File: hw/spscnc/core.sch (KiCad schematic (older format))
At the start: 55 parts, among them J11 Conn_01x04, J7 USB_B_Micro, Q11 BSP41, Q12 BSP42, U13 74HC595, U14 74HC595, U3 NCP1117ST33T3G, U4 ESP32-WROOM-32D, U8 FT232RL

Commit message: Finished preliminary routing, pending checklist and review
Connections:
- net labels added: LIM_A, LIM_B
- wire segments 118 -> 120
- no-connect marks 21 -> 19
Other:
- note removed: "CHECKS:\n[OK] change fluidnc config and attempt to boot.\n[OK] check bootmode is ok with GPIO signals\ncheck pulses during boot on output pins.\n"
- note removed: "DRV8825 design used io15 for the door\n"
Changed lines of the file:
@@
 	1    0    0    -1
 $EndComp
-Text Notes 5275 8450 0    50   ~ 0
-DRV8825 design used io15 for the door\n
 Text GLabel 7425 1975 2    39   Output ~ 0
 ~STEPPER_CS
@@
 	-1   0    0    -1
 $EndComp
-Text Notes 12650 3350 0    50   ~ 0
+Text Notes 9075 4125 0    50   ~ 0
 BOOT MODE:\nMTDI 0 => 3v3 SPI\nGPIO0 1 => Boot APP\nGPIO2 0 => Download\nMTDO 0 => Silent UART / SDIO Sample Fall\nGPIO5 SDIO Launch Fall
-Text Notes 12525 3900 0    50   ~ 0
-CHECKS:\n[OK] change fluidnc config and attempt to boot.\n[OK] check bootmode is ok with GPIO signals\ncheck pulses during boot on output pins.\n
 Text GLabel 7775 1475 2    50   Output ~ 0
 SPINDLE_EN
@@
 Wire Wire Line
 	7575 1475 7775 1475
-Text GLabel 9750 5000 2    50   Output ~ 0
+Text GLabel 9750 5100 2    50   Output ~ 0
 DIR_A
 $Comp
@@
 Wire Wire Line
 	9550 5100 9750 5100
-Text GLabel 9750 5100 2    50   Output ~ 0
+Text GLabel 9750 5300 2    50   Output ~ 0
 STEP_A
 Wire Wire Line
@@
 Wire Wire Line
 	5425 5475 5425 5950
-Text GLabel 9750 5300 2    50   Output ~ 0
+Text GLabel 9750 5000 2    50   Output ~ 0
 DIR_B
 $Comp
@@
 	7550 5775 6400 5775
 NoConn ~ 9350 5700
-NoConn ~ 7325 1775
-NoConn ~ 7325 1875
 NoConn ~ 7375 2775
 $Comp
@@
 	1    0    0    -1
 $EndComp
+Text GLabel 7400 1775 2    50   Input ~ 0
+LIM_A
+Text GLabel 7400 1875 2    50   Input ~ 0
+LIM_B
+Wire Wire Line
+	7400 1775 7325 1775
+Wire Wire Line
+	7325 1875 7400 1875
 $EndSCHEMATC

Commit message: As ordered 1.0.1
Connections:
- wire segments 120 -> 123
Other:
- note added: "CRITICAL BOOT MODE:\nMTDI 0 => 3v3 SPI\nGPIO0 1 => Boot APP\nGPIO2 0 => Download\nMTDO 0 => Silent UART / SDIO Sample Fall\nGPIO5 SDIO Launch Falling edge.\n"
- note removed: "BOOT MODE:\nMTDI 0 => 3v3 SPI\nGPIO0 1 => Boot APP\nGPIO2 0 => Download\nMTDO 0 => Silent UART / SDIO Sample Fall\nGPIO5 SDIO Launch Fall"
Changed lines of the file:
@@
 Sheet 6 17
 Title "Trinamic FluidNC CNC Controller"
-Date "2022-01-27"
-Rev "1.0.0"
+Date "2022-02-12"
+Rev "1.0.1"
 Comp ""
 Comment1 ""
@@
 $EndComp
 Text Notes 9075 4125 0    50   ~ 0
-BOOT MODE:\nMTDI 0 => 3v3 SPI\nGPIO0 1 => Boot APP\nGPIO2 0 => Download\nMTDO 0 => Silent UART / SDIO Sample Fall\nGPIO5 SDIO Launch Fall
+CRITICAL BOOT MODE:\nMTDI 0 => 3v3 SPI\nGPIO0 1 => Boot APP\nGPIO2 0 => Download\nMTDO 0 => Silent UART / SDIO Sample Fall\nGPIO5 SDIO Launch Falling edge.\n
 Text GLabel 7775 1475 2    50   Output ~ 0
 SPINDLE_EN
 Text GLabel 8650 2875 2    50   Output ~ 0
 ENABLE_STEPPERS
-Text GLabel 7800 2075 2    50   Output ~ 0
+Text GLabel 8750 2075 2    50   Output ~ 0
 SPINDLE_PWM
 Text GLabel 9750 4800 2    50   Output ~ 0
@@
 Text Label 5600 5375 2    50   ~ 0
 I2S_WORDSTROBE
-$Comp
-L power:GND-power #PWR?
-U 1 1 62063E5C
-P 5600 5175
-AR Path="/5AD46BE5/62063E5C" Ref="#PWR?"  Part="1"
-AR Path="/5AD46BE5/619A452E/62063E5C" Ref="#PWR?"  Part="1"
-AR Path="/62063E5C" Ref="#PWR?"  Part="1"
-AR Path="/61B9A8A6/62063E5C" Ref="#PWR?"  Part="1"
-AR Path="/61C743E7/61B9A8A6/62063E5C" Ref="#PWR?"  Part="1"
-AR Path="/61C81F9D/62063E5C" Ref="#PWR024"  Part="1"
-F 0 "#PWR024" H 5600 4925 50  0001 C CNN
-F 1 "GND" H 5600 5025 50  0000 C CNN
-F 2 "" H 5600 5175 50  0001 C CNN
-F 3 "" H 5600 5175 50  0001 C CNN
-	1    5600 5175
-	0    1    -1   0
-$EndComp
 Text Label 5600 5475 2    50   ~ 0
 ~I2S_ENABLE
@@
 	9750 4800 9550 4800
 Wire Wire Line
-	7600 2075 7800 2075
+	7600 2075 8750 2075
 Wire Wire Line
 	7575 1475 7775 1475
@@
 Text Label 8550 5300 2    50   ~ 0
 I2S_WORDSTROBE
-$Comp
-L power:GND-power #PWR?
-U 1 1 620F09C1
-P 8550 5100
-AR Path="/5AD46BE5/620F09C1" Ref="#PWR?"  Part="1"
-AR Path="/5AD46BE5/619A452E/620F09C1" Ref="#PWR?"  Part="1"
-AR Path="/620F09C1" Ref="#PWR?"  Part="1"
-AR Path="/61B9A8A6/620F09C1" Ref="#PWR?"  Part="1"
-AR Path="/61C743E7/61B9A8A6/620F09C1" Ref="#PWR?"  Part="1"
-AR Path="/61C81F9D/620F09C1" Ref="#PWR083"  Part="1"
-F 0 "#PWR083" H 8550 4850 50  0001 C CNN
-F 1 "GND" H 8550 4950 50  0000 C CNN
-F 2 "" H 8550 5100 50  0001 C CNN
-F 3 "" H 8550 5100 50  0001 C CNN
-	1    8550 5100
-	0    1    -1   0
-$EndComp
 Text Label 8550 5400 2    50   ~ 0
 ~I2S_ENABLE
@@
 Wire Wire Line
 	7325 1875 7400 1875
+$Comp
+L power:+3.3VA-power #PWR?
+U 1 1 620826BE
+P 7975 5050
+AR Path="/61367F02/620826BE" Ref="#PWR?"  Part="1"
+AR Path="/5AD46BE5/619A452E/61B9A8A6/620826BE" Ref="#PWR?"  Part="1"
+AR Path="/61B9A8A6/620826BE" Ref="#PWR?"  Part="1"
+AR Path="/61C743E7/61B9A8A6/620826BE" Ref="#PWR?"  Part="1"
+AR Path="/61C81F9D/620826BE" Ref="#PWR?"  Part="1"
+AR Path="/620826BE" Ref="#PWR?"  Part="1"
+F 0 "#PWR?" H 7975 4900 50  0001 C CNN
+F 1 "+3.3VA" H 7975 5225 50  0000 C CNN
+F 2 "" H 7975 5050 50  0001 C CNN
+F 3 "" H 7975 5050 50  0001 C CNN
+	1    7975 5050
+	1    0    0    -1
+$EndComp
+Wire Wire Line
+	8550 5100 7975 5100
+Wire Wire Line
+	7975 5100 7975 5050
+$Comp
+L power:+3.3VA-power #PWR?
+U 1 1 6208D205
+P 5200 5175
+AR Path="/61367F02/6208D205" Ref="#PWR?"  Part="1"
+AR Path="/5AD46BE5/619A452E/61B9A8A6/6208D205" Ref="#PWR?"  Part="1"
+AR Path="/61B9A8A6/6208D205" Ref="#PWR?"  Part="1"
+AR Path="/61C743E7/61B9A8A6/6208D205" Ref="#PWR?"  Part="1"
+AR Path="/61C81F9D/6208D205" Ref="#PWR?"  Part="1"
+AR Path="/6208D205" Ref="#PWR?"  Part="1"
+F 0 "#PWR?" H 5200 5025 50  0001 C CNN
+F 1 "+3.3VA" V 5225 5425 50  0000 C CNN
+F 2 "" H 5200 5175 50  0001 C CNN
+F 3 "" H 5200 5175 50  0001 C CNN
+	1    5200 5175
+	0    -1   -1   0
+$EndComp
+Wire Wire Line
+	5200 5175 5600 5175
 $EndSCHEMATC

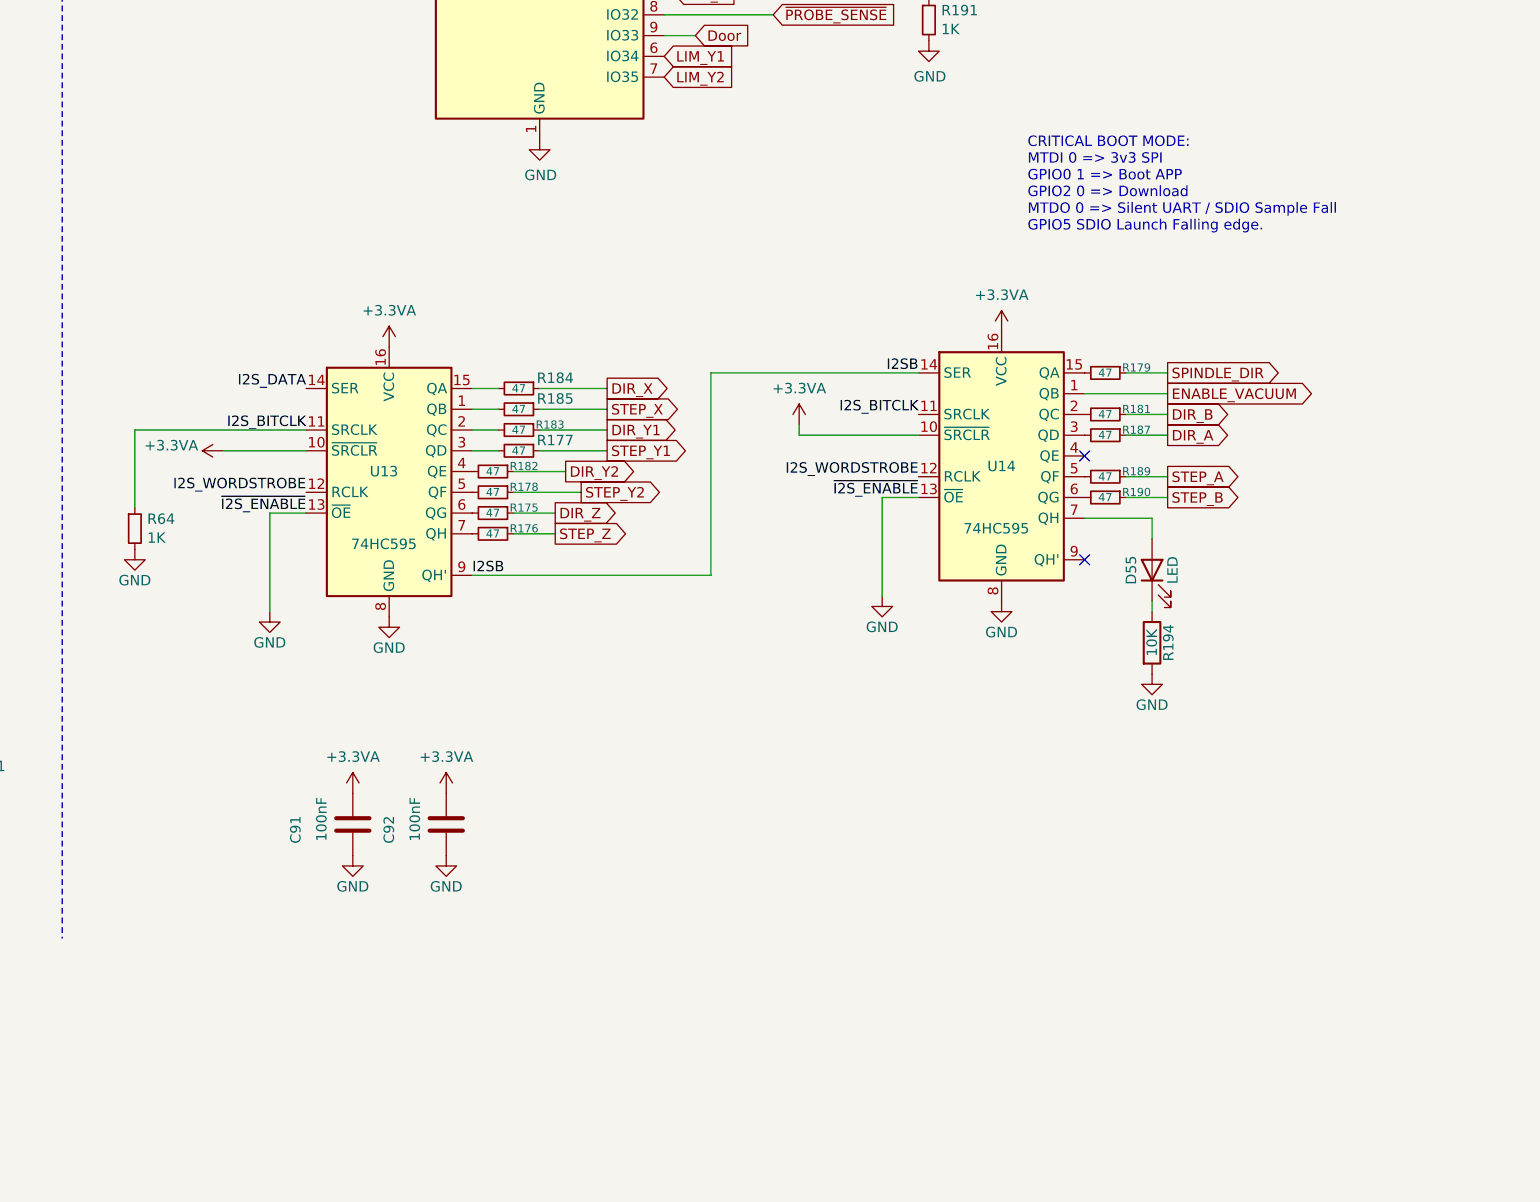
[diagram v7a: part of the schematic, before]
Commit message: Prototype corrections without new PCB
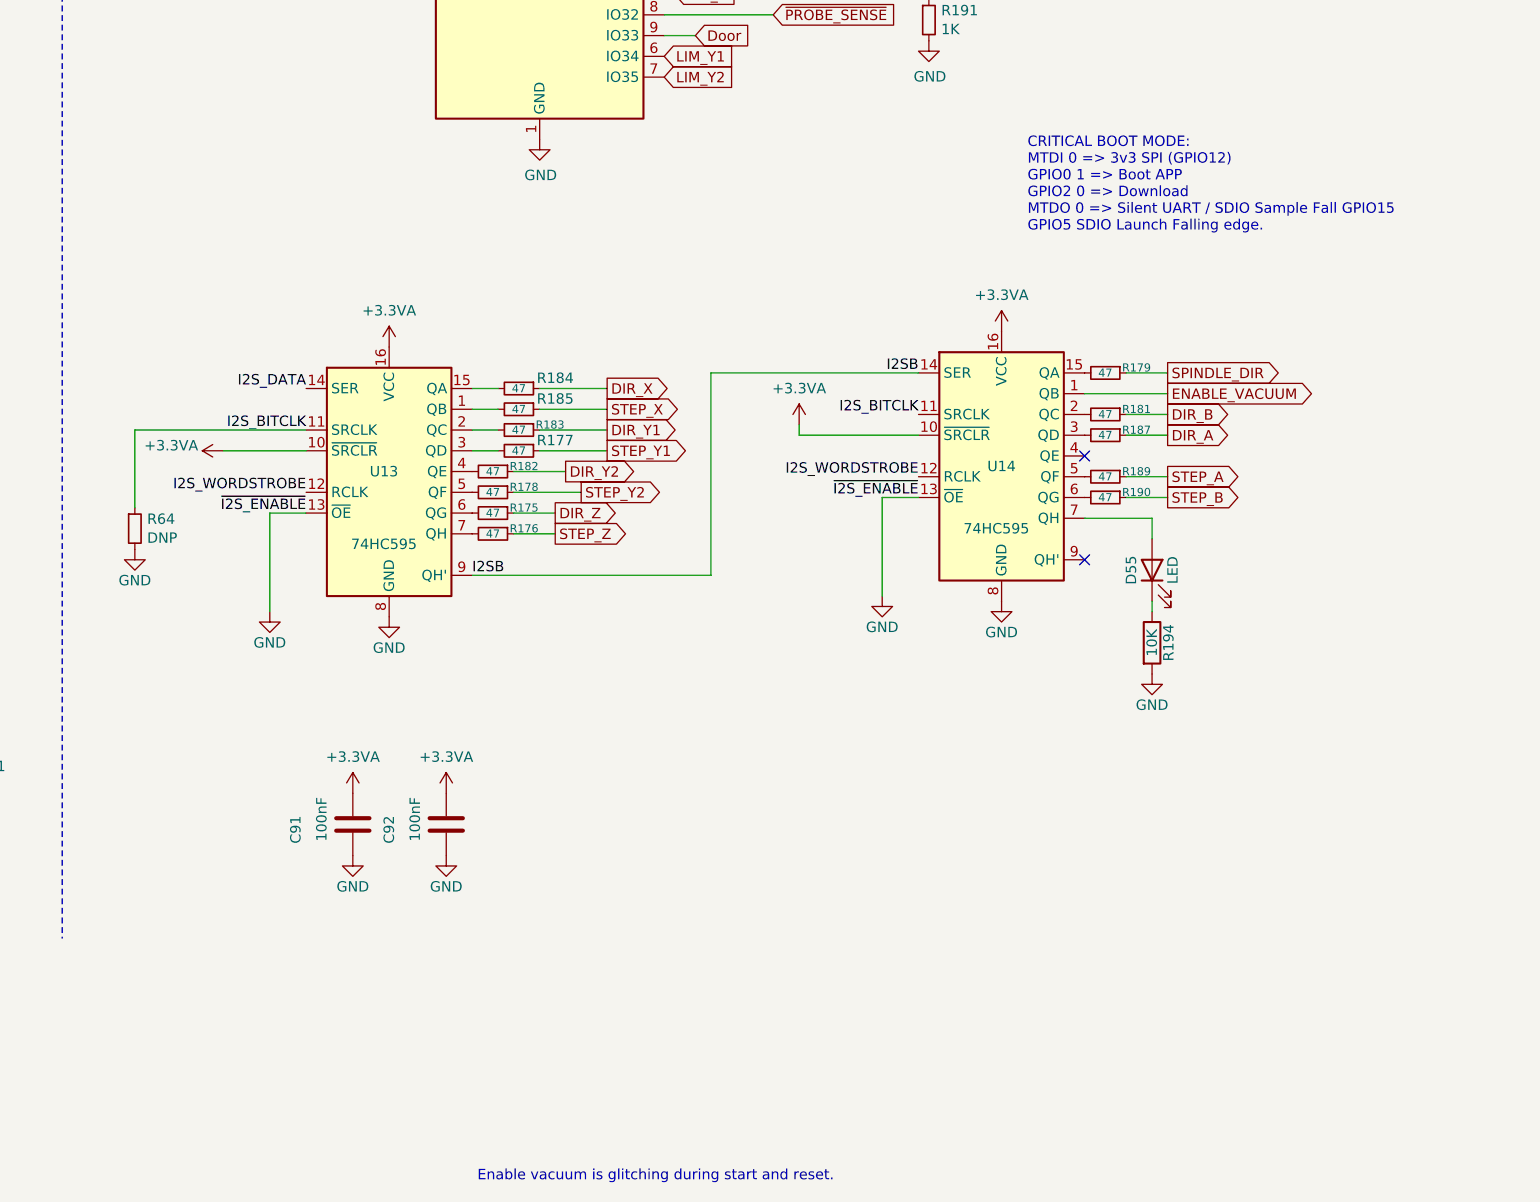
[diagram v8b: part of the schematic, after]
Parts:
- R64: value 1K -> DNP; jlcpcb C21190 -> DNP654
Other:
- note added: "CRITICAL BOOT MODE:\nMTDI 0 => 3v3 SPI (GPIO12)\nGPIO0 1 => Boot APP\nGPIO2 0 => Download\nMTDO 0 => Silent UART / SDIO Sample Fall GPIO15\nGPIO5 SDIO Launch Falling edge.\n"
- note added: "Enable vacuum is glitching during start and reset."
- note removed: "CRITICAL BOOT MODE:\nMTDI 0 => 3v3 SPI\nGPIO0 1 => Boot APP\nGPIO2 0 => Download\nMTDO 0 => Silent UART / SDIO Sample Fall\nGPIO5 SDIO Launch Falling edge.\n"
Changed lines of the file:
@@
 $EndComp
 Text Notes 9075 4125 0    50   ~ 0
-CRITICAL BOOT MODE:\nMTDI 0 => 3v3 SPI\nGPIO0 1 => Boot APP\nGPIO2 0 => Download\nMTDO 0 => Silent UART / SDIO Sample Fall\nGPIO5 SDIO Launch Falling edge.\n
+CRITICAL BOOT MODE:\nMTDI 0 => 3v3 SPI (GPIO12)\nGPIO0 1 => Boot APP\nGPIO2 0 => Download\nMTDO 0 => Silent UART / SDIO Sample Fall GPIO15\nGPIO5 SDIO Launch Falling edge.\n
 Text GLabel 7775 1475 2    50   Output ~ 0
 SPINDLE_EN
@@
 AR Path="/61C81F9D/62063E7E" Ref="R64"  Part="1"
 F 0 "R64" H 4834 5596 50  0000 L CNN
-F 1 "1K" H 4834 5505 50  0000 L CNN
+F 1 "DNP" H 4834 5505 50  0000 L CNN
 F 2 "Resistor_SMD:R_0603_1608Metric" H 4775 5550 50  0001 C CNN
 F 3 "~" H 4775 5550 50  0001 C CNN
-F 4 "C21190" H 4775 5550 50  0001 C CNN "jlcpcb"
+F 4 "DNP654" H 4775 5550 50  0001 C CNN "jlcpcb"
 	1    4775 5550
 	1    0    0    -1
@@
 Wire Wire Line
 	5200 5175 5600 5175
+Text Notes 6425 8700 0    50   ~ 0
+Enable vacuum is glitching during start and reset.
 $EndSCHEMATC
